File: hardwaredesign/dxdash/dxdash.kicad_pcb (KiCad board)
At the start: 2 copper layers, 104.6 x 90.6 mm, 139 parts, among them J1 Conn_01x08_Pin, J10 Screw_Terminal_01x04, J11 Screw_Terminal_01x04, J13 Conn_01x01_Pin, J16 uC_NRST, J17 3V3_uC, J18 SWO, J3 Screw_Terminal_01x04, J4 DEBUG, J5 UART, J7 Screw_Terminal_01x04, J9 Screw_Terminal_01x04, Q1 NCV8402xST, Q2 NCV8402xST, Q3 NCV8402xST, Q4 BC556, Q6 BC546, Q7 BC556, Q8 BC546, SW1 SW_Push, SW2 SW_Push, SW3 SW_Push, SW4 SW_Push, SW5 SW_Push, U2 SN65HVD234, U3 STM32F103RETx, U4 TPS54302, U6 AMS1117-3.3, U7 74HCT04, Y2 8MHz

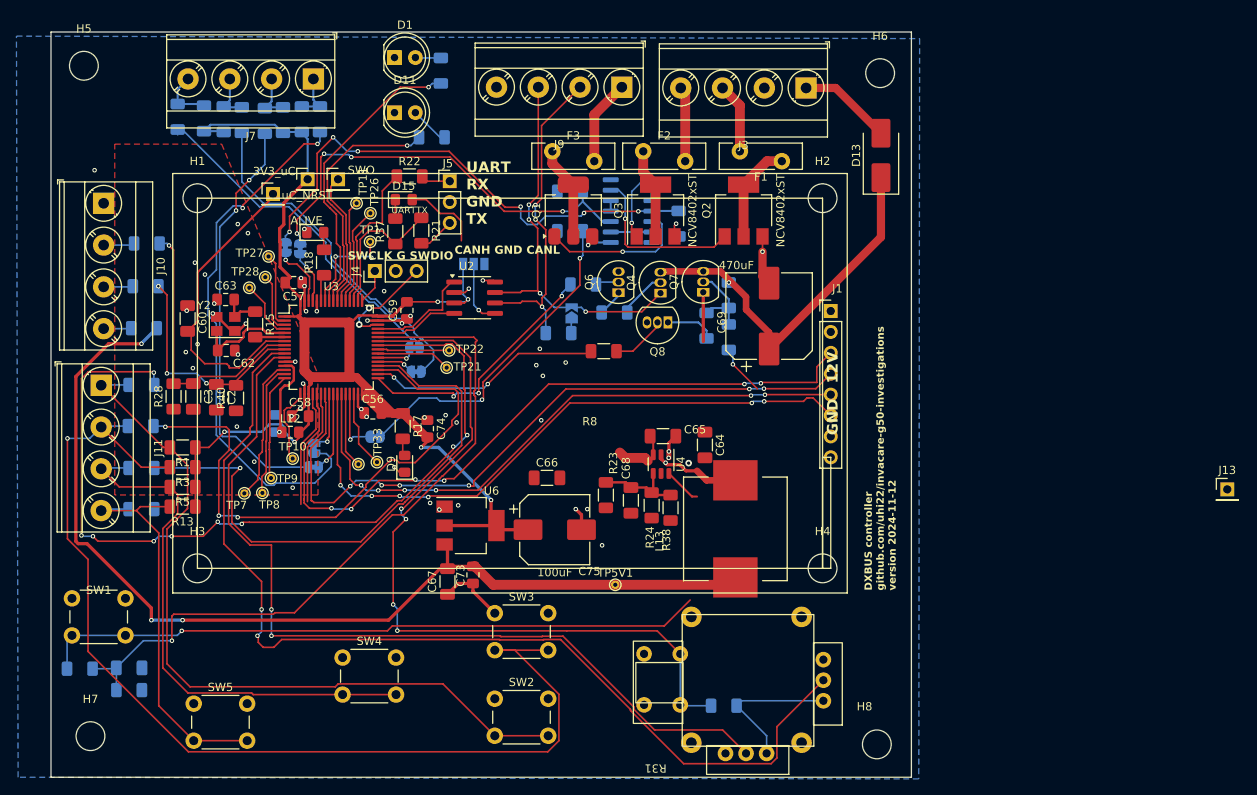
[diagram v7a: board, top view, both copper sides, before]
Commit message: board: layout finished
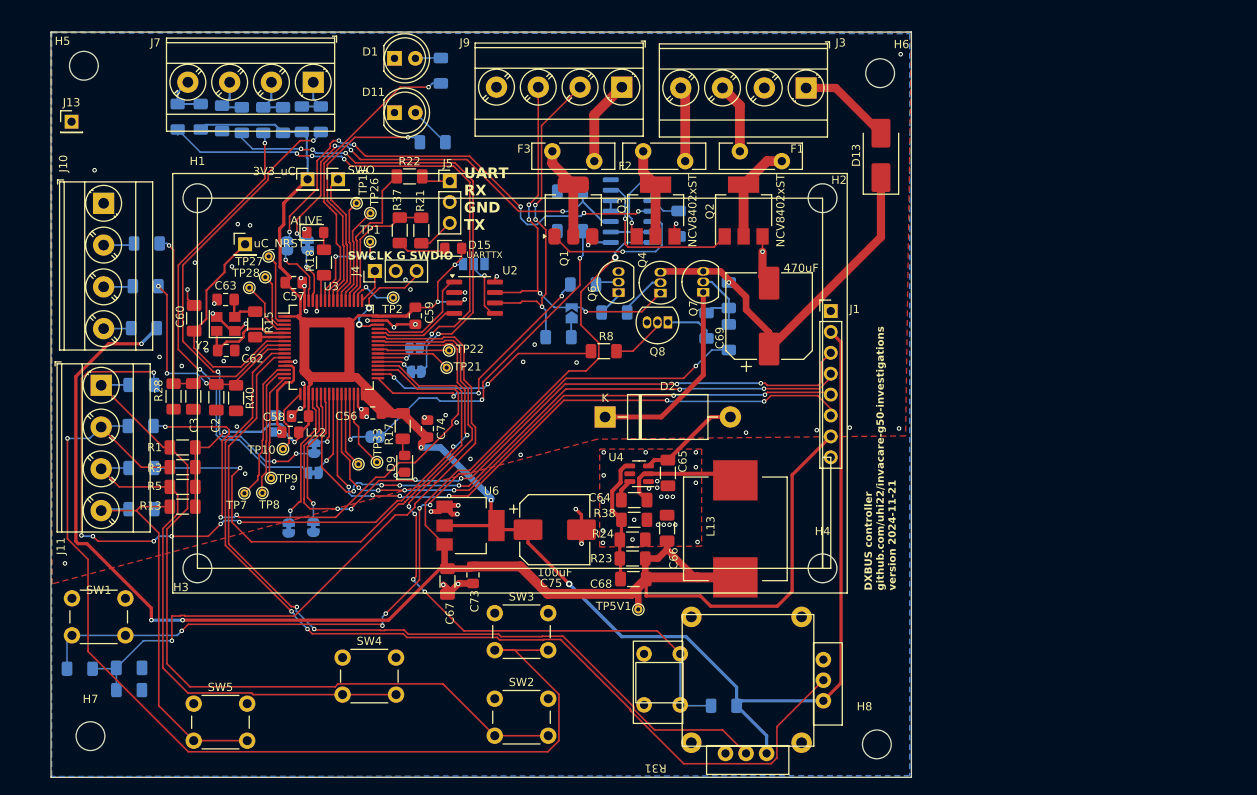
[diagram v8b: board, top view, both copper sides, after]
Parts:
- added D2: Zener 5V, Diode_THT:D_DO-201_P15.24mm_Horizontal, F.Cu at (189.4, 115.4)
- added JP10: SolderJumper_2_Bridged, Jumper:SolderJumper-2_P1.3mm_Bridged_RoundedPad1.0x1.5mm, B.Cu at (150.9, 128.9)
- added JP11: SolderJumper_2_Bridged, Jumper:SolderJumper-2_P1.3mm_Bridged_RoundedPad1.0x1.5mm, B.Cu at (153.9, 128.8)
- added TP2: ~, TestPoint:TestPoint_THTPad_D1.0mm_Drill0.5mm, F.Cu at (163.6, 100.9)
- moved J13 147.4 mm to (124.5, 79.5)
- moved C66 15.8 mm to (196.9, 128.9), turned to -90 degrees
- moved C64 10.9 mm to (192.9, 125.5), turned to 180 degrees
- moved C68 9.57 mm to (192.8, 135.1), turned to 0 degrees
- moved D15 8.44 mm to (170.9, 94.9)
- moved R23 8.36 mm to (192.7, 132.6), turned to 180 degrees
- moved J16 6.99 mm to (145.6, 94.4)
- moved R24 4.77 mm to (192.7, 130.3), turned to 180 degrees
- moved R38 4.66 mm to (192.9, 127.9), turned to 180 degrees
- moved C65 4.51 mm to (197.0, 122.2), turned to 90 degrees
- moved TP5V1 4.10 mm to (193.4, 138.8)
- moved U4 2.91 mm to (193.5, 122.3), turned to 180 degrees
- moved TP10 1.65 mm to (150.2, 119.3)
- moved C59 1.22 mm to (166.3, 103.1)
- moved JP1 1.01 mm to (153.2, 94.5)
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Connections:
- Q7 pad 1: 24V_SWITCHED -> Net-(D2-K)
- U3 pad 50: unconnected-(U3-PA15-Pad50) -> Net-(U3-PA15)
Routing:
- net 5V: track 124.0 -> 238.8 mm, vias 3 -> 4
- net 3V3_uC: track 209.8 -> 287.7 mm, vias 6 -> 8
- net Net-(D2-K): track 0.00 -> 24.1 mm
- net uC_switch4: track 42.5 -> 63.1 mm, vias 0 -> 4
- net Net-(R10-Pad2): track 87.4 -> 104.6 mm, vias 2 -> 6
- net uC_switch3: track 42.5 -> 57.7 mm, vias 0 -> 4
- net uC_NRST: track 37.4 -> 28.4 mm
- net uC_joystickbutton: track 95.7 -> 89.2 mm
- net Net-(U3-PA15): track 0.00 -> 5.98 mm, vias 0 -> 1
- net uC_joystickX: track 123.4 -> 117.8 mm
- net uC_switch1: track 65.6 -> 60.2 mm, vias 2 -> 4
- net SPI1_MOSI: track 84.4 -> 79.2 mm
- net uC_switch2: track 51.2 -> 56.3 mm
- net Net-(U4-FB): track 10.9 -> 15.6 mm
- net uC_joystickY: track 104.9 -> 100.3 mm
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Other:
- board text added: "24V"
- board text added: "BTN1 2 3 4"
- board text added: "CANH"
- board text added: "CANL"
- board text added: "DXBUS controller github.com/uhi22/invacare-g50-investigations version 2024-11-21"
- board text added: "GND"
- board text added: "GND 1 2 POT5V"
- board text added: "OUT1"
- board text added: "OUT2"
- board text added: "OUT3"
- board text added: "SWT 1 2 3 4"
- board text added: "nc"
- board text removed: "CANH GND CANL"
- board text removed: "DXBUS controller github.com/uhi22/invacare-g50-investigations version 2024-11-12"
- board text removed: "GND 12V"
